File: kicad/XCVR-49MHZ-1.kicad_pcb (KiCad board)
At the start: 4 copper layers, 55 x 35 mm, 0 parts

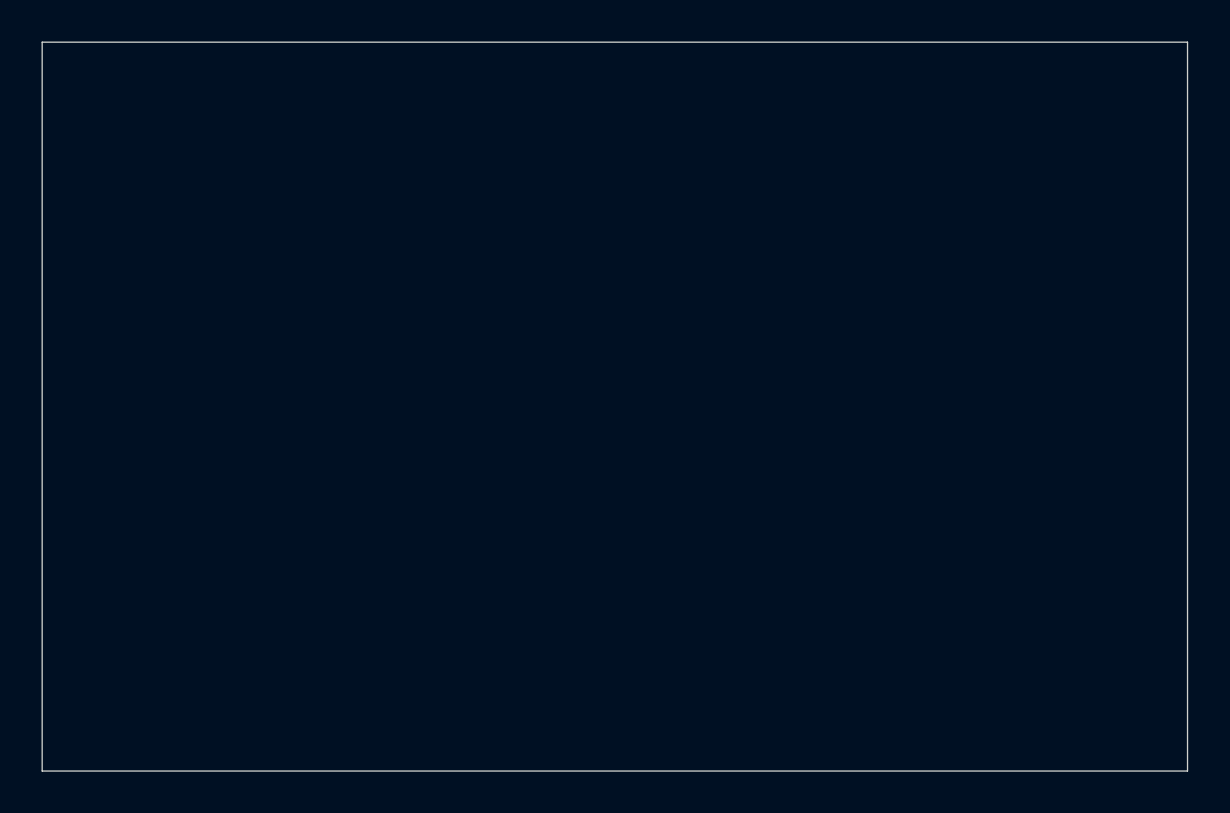
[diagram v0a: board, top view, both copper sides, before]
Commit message: updated the xcvr to fix drc issues an
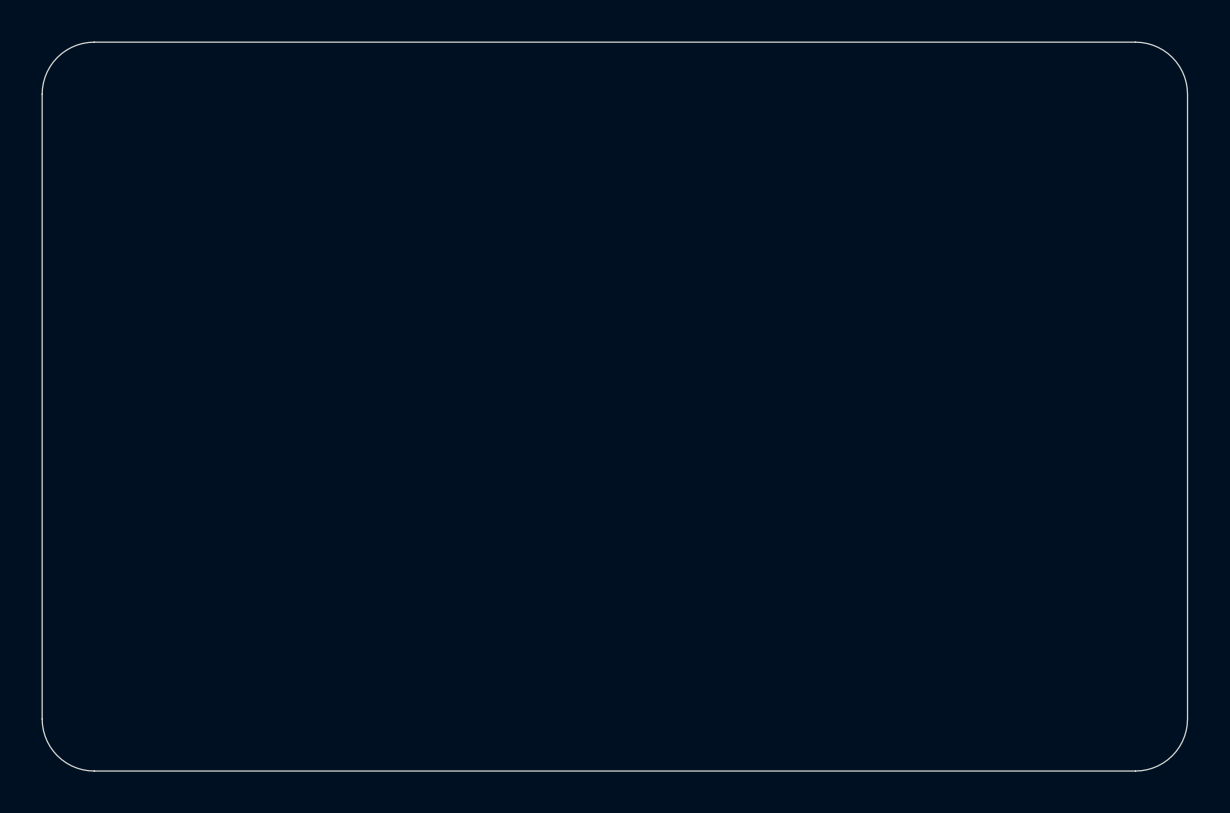
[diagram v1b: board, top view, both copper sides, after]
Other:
- outline, holes or cut-outs redrawn
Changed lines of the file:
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@@
 	(net 14 "AFSK_OUT")
 	(net 15 "AFSK_IN")
-     (gr_rect
-		(start 100 100) (end 155 135)
-		(stroke (width 0.05) (type solid))
+	(gr_arc
+		(start 100 102.5)
+		(mid 100.73223 100.73223)
+		(end 102.5 100)
+		(stroke
+			(width 0.05)
+			(type solid)
+		)
 		(layer "Edge.Cuts")
 	)
+	(gr_line
+		(start 102.5 100)
+		(end 152.5 100)
+		(stroke
+			(width 0.05)
+			(type solid)
+		)
+		(layer "Edge.Cuts")
+	)
+	(gr_arc
+		(start 152.5 100)
+		(mid 154.26777 100.73223)
+		(end 155 102.5)
+		(stroke
+			(width 0.05)
+			(type solid)
+		)
+		(layer "Edge.Cuts")
+	)
+	(gr_line
+		(start 155 102.5)
+		(end 155 132.5)
+		(stroke
+			(width 0.05)
+			(type solid)
+		)
+		(layer "Edge.Cuts")
+	)
+	(gr_arc
+		(start 155 132.5)
+		(mid 154.26777 134.26777)
+		(end 152.5 135)
+		(stroke
+			(width 0.05)
+			(type solid)
+		)
+		(layer "Edge.Cuts")
+	)
+	(gr_line
+		(start 152.5 135)
+		(end 102.5 135)
+		(stroke
+			(width 0.05)
+			(type solid)
+		)
+		(layer "Edge.Cuts")
+	)
+	(gr_arc
+		(start 102.5 135)
+		(mid 100.73223 134.26777)
+		(end 100 132.5)
+		(stroke
+			(width 0.05)
+			(type solid)
+		)
+		(layer "Edge.Cuts")
+	)
+	(gr_line
+		(start 100 132.5)
+		(end 100 102.5)
+		(stroke
+			(width 0.05)
+			(type solid)
+		)
+		(layer "Edge.Cuts")
+	)
